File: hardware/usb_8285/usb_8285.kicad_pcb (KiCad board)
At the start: 2 copper layers, 18.4 x 12.1 mm, 24 parts, among them P1 UTX, P10 ADC, P2 URX, P3 D+, P4 +5V, P5 +5V, P6 GND, P7 GND, P8 D-, P9 G0, U1 ESP8285, U2 1824, X1 26MHz

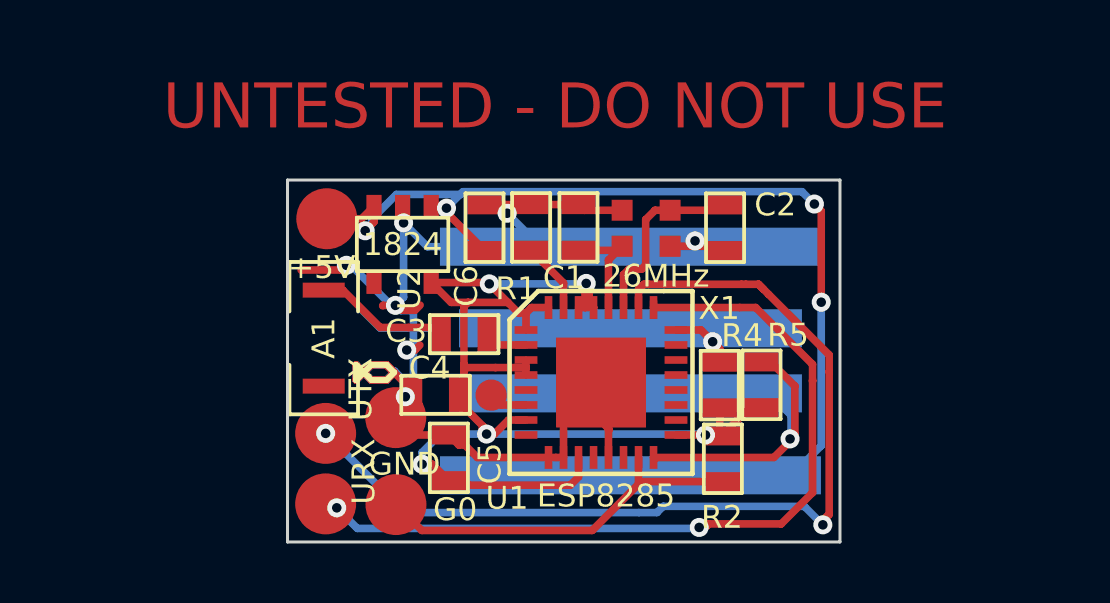
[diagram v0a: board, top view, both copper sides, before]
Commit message: update hardware - yes, it works!
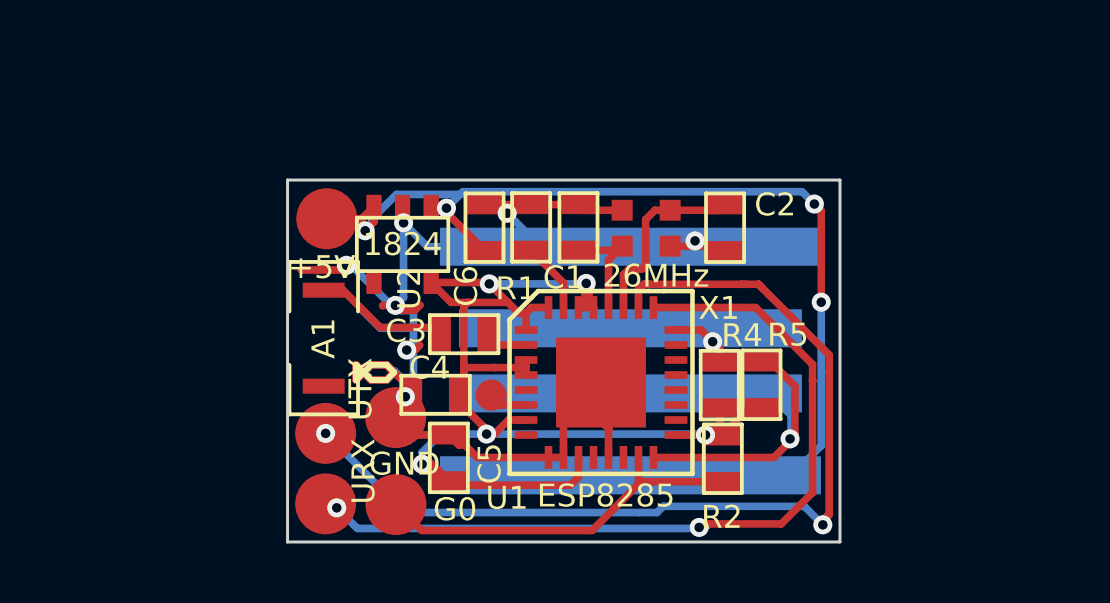
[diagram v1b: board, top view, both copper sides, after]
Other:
- board text added: "Tested working 2016-08-26 C.L. NOTE: Do not populate R4."
- board text removed: "UNTESTED - DO NOT USE"
